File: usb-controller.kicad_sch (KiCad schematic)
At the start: 47 parts, among them Q1502 PJE138K, Q1503 PJE138K, U1501 UPD720201K8-701-BAC-A, U1502 W25Q80DV_USON, Y1501 Resonator_24MHz_ECX-1247

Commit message: [#100501] Reannotate schematic
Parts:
- renumbered C1501 to C105, C1502 to C106, C1503 to C107, C1504 to C108, C1505 to C109, C1506 to C110, C1507 to C111, C1508 to C112, C1509 to C113, C1510 to C114, C1511 to C115, C1512 to C116, C1513 to C117, C1514 to C118, C1515 to C119, C1516 to C120, C1517 to C121, C1518 to C122, C1519 to C123, C1520 to C124, C1521 to C125, C1522 to C126, C1526 to C127, C1527 to C128, C1524 to C129, FB1501 to FB1, Q1503 to Q2, Q1502 to Q3, R1515 to R153, R1517 to R154, R1514 to R155, R1501 to R156, R1516 to R157, R1512 to R158, R1513 to R159, R1503 to R160, R1504 to R161, R1505 to R162, R1506 to R163, R1507 to R164, R1508 to R165, TP1501 to TP20, TP1502 to TP21, TP1503 to TP22, U1501 to U19, U1502 to U20, Y1501 to Y1

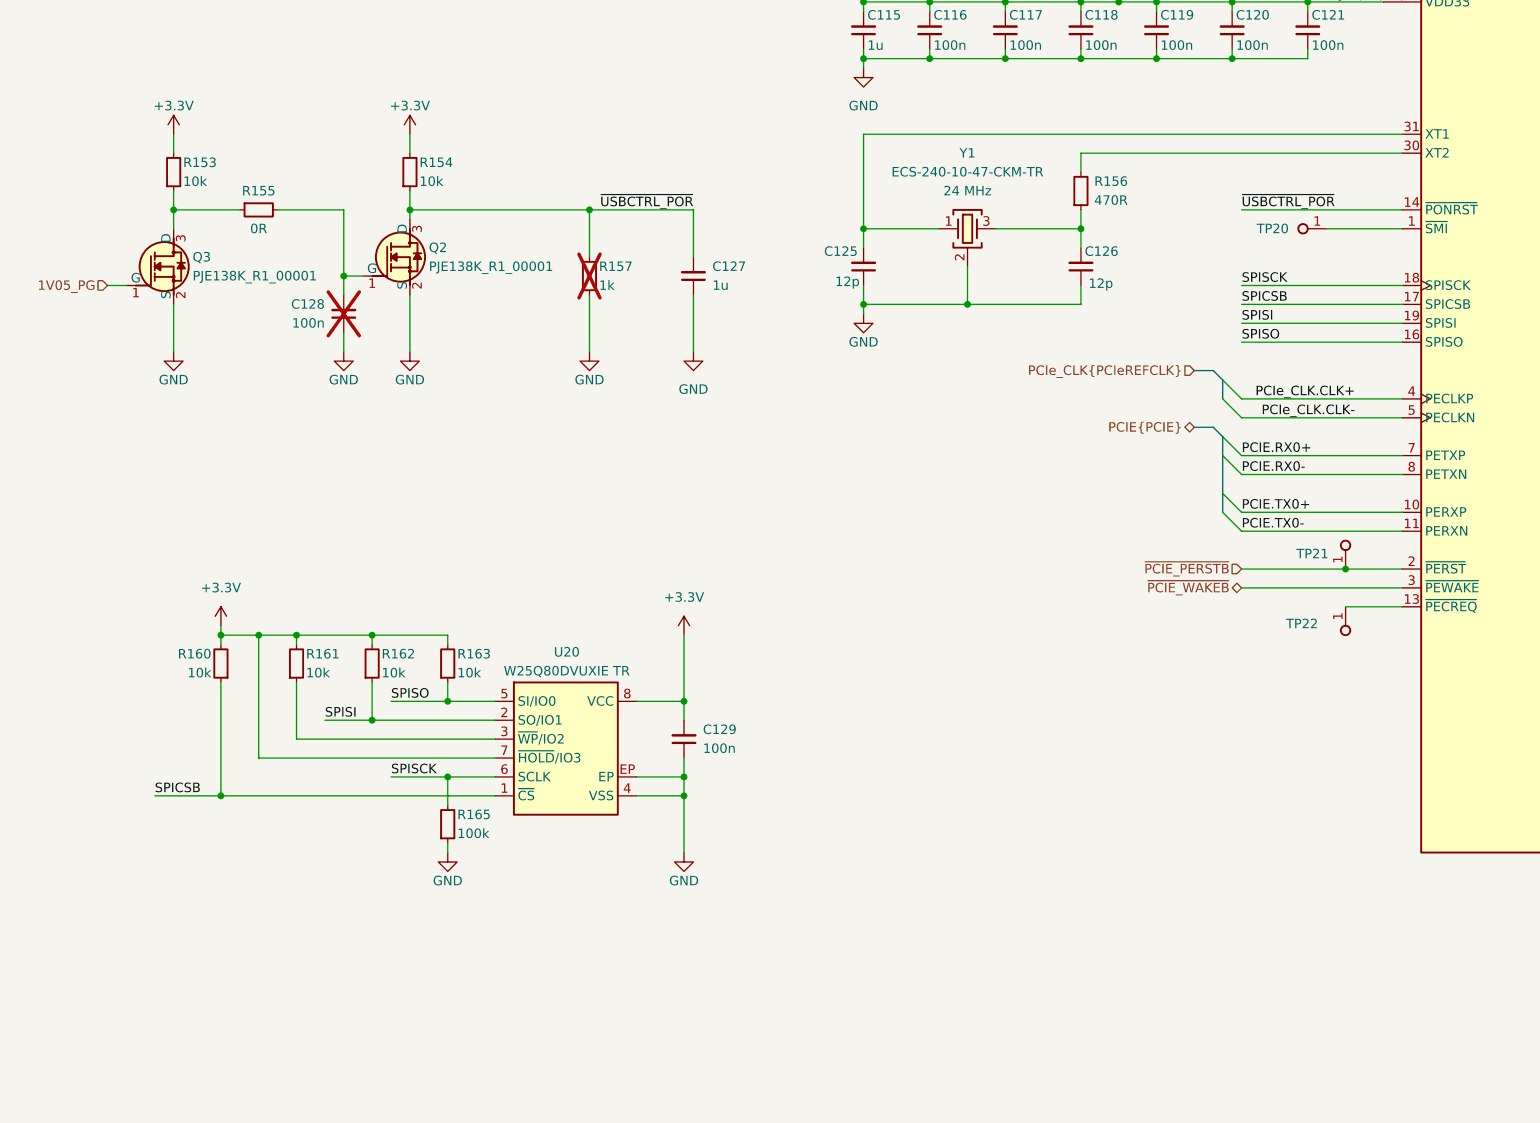
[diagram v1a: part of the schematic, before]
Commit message: [#100501] Add missing pullup resistors for USB controller, add Tag-Connect for its FLASH
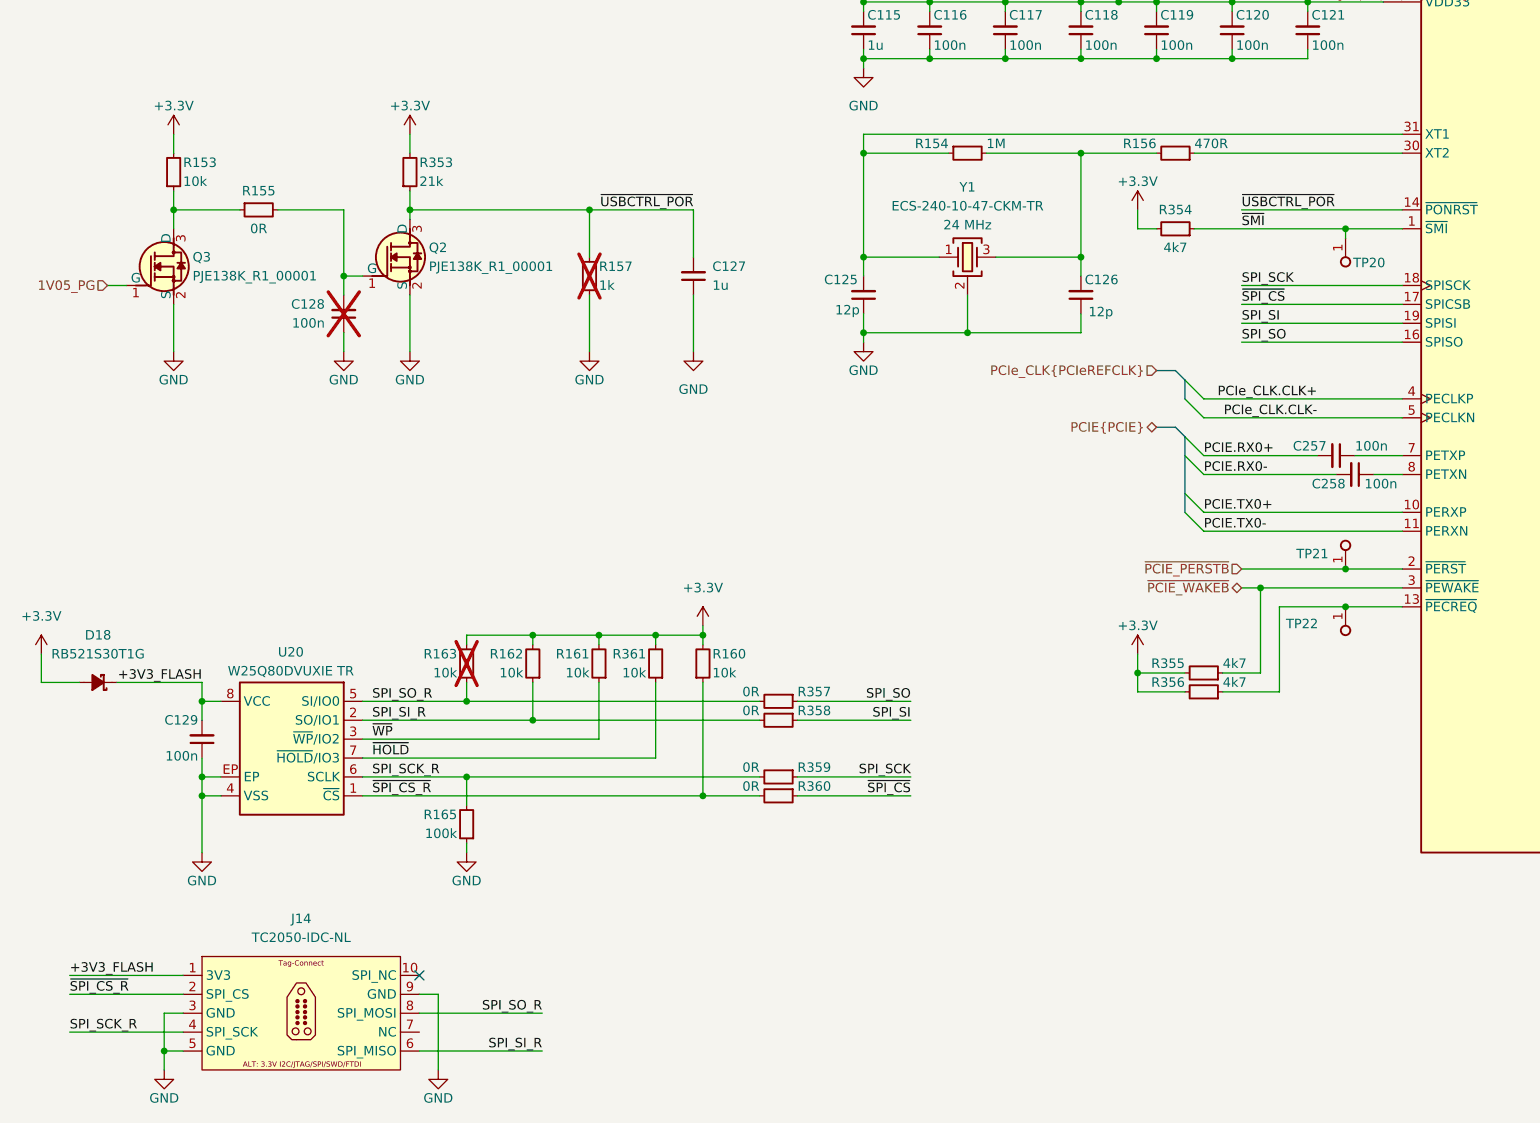
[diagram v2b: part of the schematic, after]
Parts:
- removed R154: R_10k_0402, antmicro-footprints:R_0402_1005Metric, symbol antmicroResistors0402:R_10k_0402
- added C257, C258: C_100n_16V_X7R_0402, antmicro-footprints:C_0402_1005Metric, symbol antmicroCapacitors0402:C_100n_16V_X7R_0402
- added D18: RB521S30T1G, antmicro-footprints:SOD-523, symbol antmicroDiodesRectifiersSingle:RB521S30T1G
- added J14: Tag-Connect_TC2050-IDC-NL_2x5_P1.27mm, antmicro-footprints:Tag-Connect_TC2050-IDC-NL_2x5_P1.27mm, symbol antmicroTestPoints:Tag-Connect_TC2050-IDC-NL_2x5_P1.27mm
- added R154: R_1M_0402, antmicro-footprints:R_0402_1005Metric, symbol antmicroResistors0402:R_1M_0402
- added R353: R_21k_0402, antmicro-footprints:R_0402_1005Metric, symbol antmicroResistors0402:R_21k_0402
- added R354, R355, R356: R_4k7_0402, antmicro-footprints:R_0402_1005Metric, symbol antmicroResistors0402:R_4k7_0402
- added R357, R358, R359, R360: R_0R_0402, antmicro-footprints:R_0402_1005Metric, symbol antmicroResistors0402:R_0R_0402
- added R361: R_10k_0402, antmicro-footprints:R_0402_1005Metric, symbol antmicroResistors0402:R_10k_0402
- R163: now not fitted
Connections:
- net +3.3V: now also D18.2 (A), R353.2, R354.2, R355.2, R356.2, R361.2; no longer C129.2, U20.7 (~{HOLD}/IO3), U20.8 (VCC)
- net GND: now also J14.3, J14.5, J14.9
- net PCIE.RX0+: now also C257.2; no longer U19.7 (PETXP)
- net PCIE.RX0-: now also C258.2; no longer U19.8 (PETXN)
- net ~{PCIE_WAKEB}: now also R355.1
- net ~{USBCTRL_POR}: now also R353.1
- net at C125.2, U19.31 (XT1), Y1.1: now also R154.1
- net at C126.2, Y1.3: now also R156.2, R154.2; no longer R156.1
- net at TP22.1, U19.13 (~{PECREQ}): now also R356.1
- net ~{SMI}: now reaches TP20.1, U19.1 (~{SMI})
- net ~{SMI}: now also R354.1
- net at U19.30 (XT2): now also R156.1; no longer R156.2
- net ~{WP}: now reaches R161.1, U20.3 (~{WP}/IO2)
- net SPICSB renamed ~{SPI_CS_R}
- net ~{SPI_CS_R}: now also J14.2, R360.2; no longer U19.17 (SPICSB)
- net SPISCK renamed SPI_SCK_R
- net SPI_SCK_R: now also J14.4, R359.2; no longer U19.18 (SPISCK)
- net SPISI renamed SPI_SI_R
- net SPI_SI_R: now also J14.6, R358.2; no longer U19.19 (SPISI)
- net SPISO renamed SPI_SO_R
- net SPI_SO_R: now also J14.8, R357.2; no longer U19.16 (SPISO)
- new net: C258.1, U19.8 (PETXN)
- new net: C257.1, U19.7 (PETXP)
- new net +3V3_FLASH: C129.2, D18.1 (C), J14.1, U20.8 (VCC)
- new net SPI_SCK: R359.1, U19.18 (SPISCK)
- new net SPI_SI: R358.1, U19.19 (SPISI)
- new net SPI_SO: R357.1, U19.16 (SPISO)
- new net ~{HOLD}: R361.1, U20.7 (~{HOLD}/IO3)
- new net ~{SPI_CS}: R360.1, U19.17 (SPICSB)
- no-connect marks 6 -> 7
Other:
- moved on the sheet: C125, C126, C129, R160, R161, R162, R165, TP20, U20, Y1

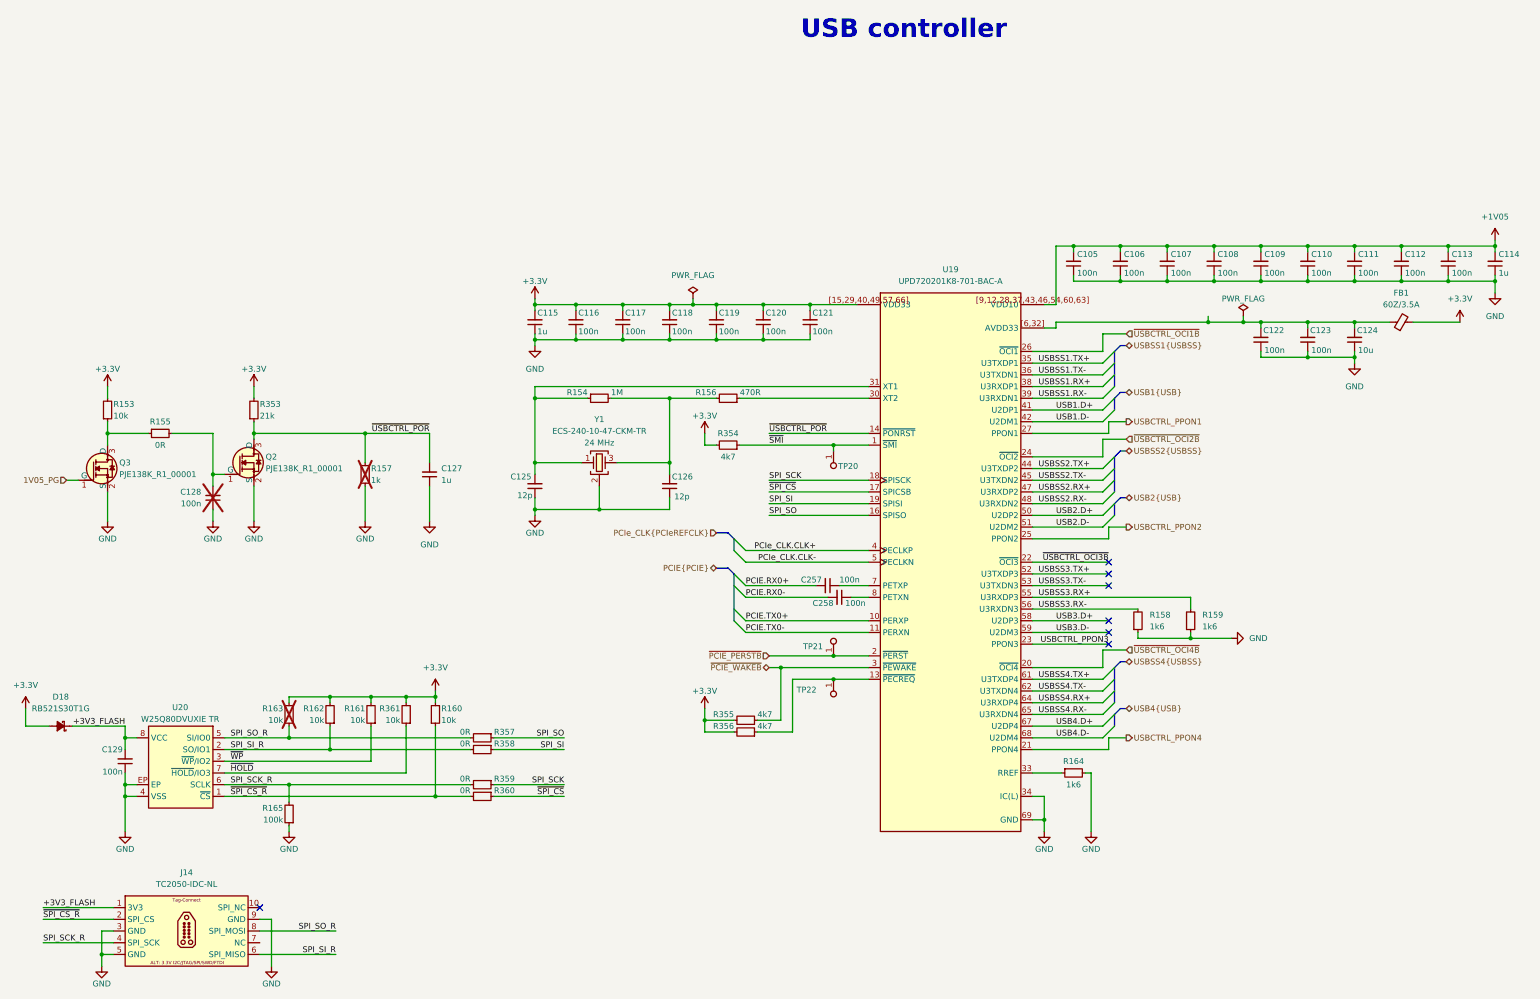
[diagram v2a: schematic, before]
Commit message: [#100501] Improve USB controller schematic readability
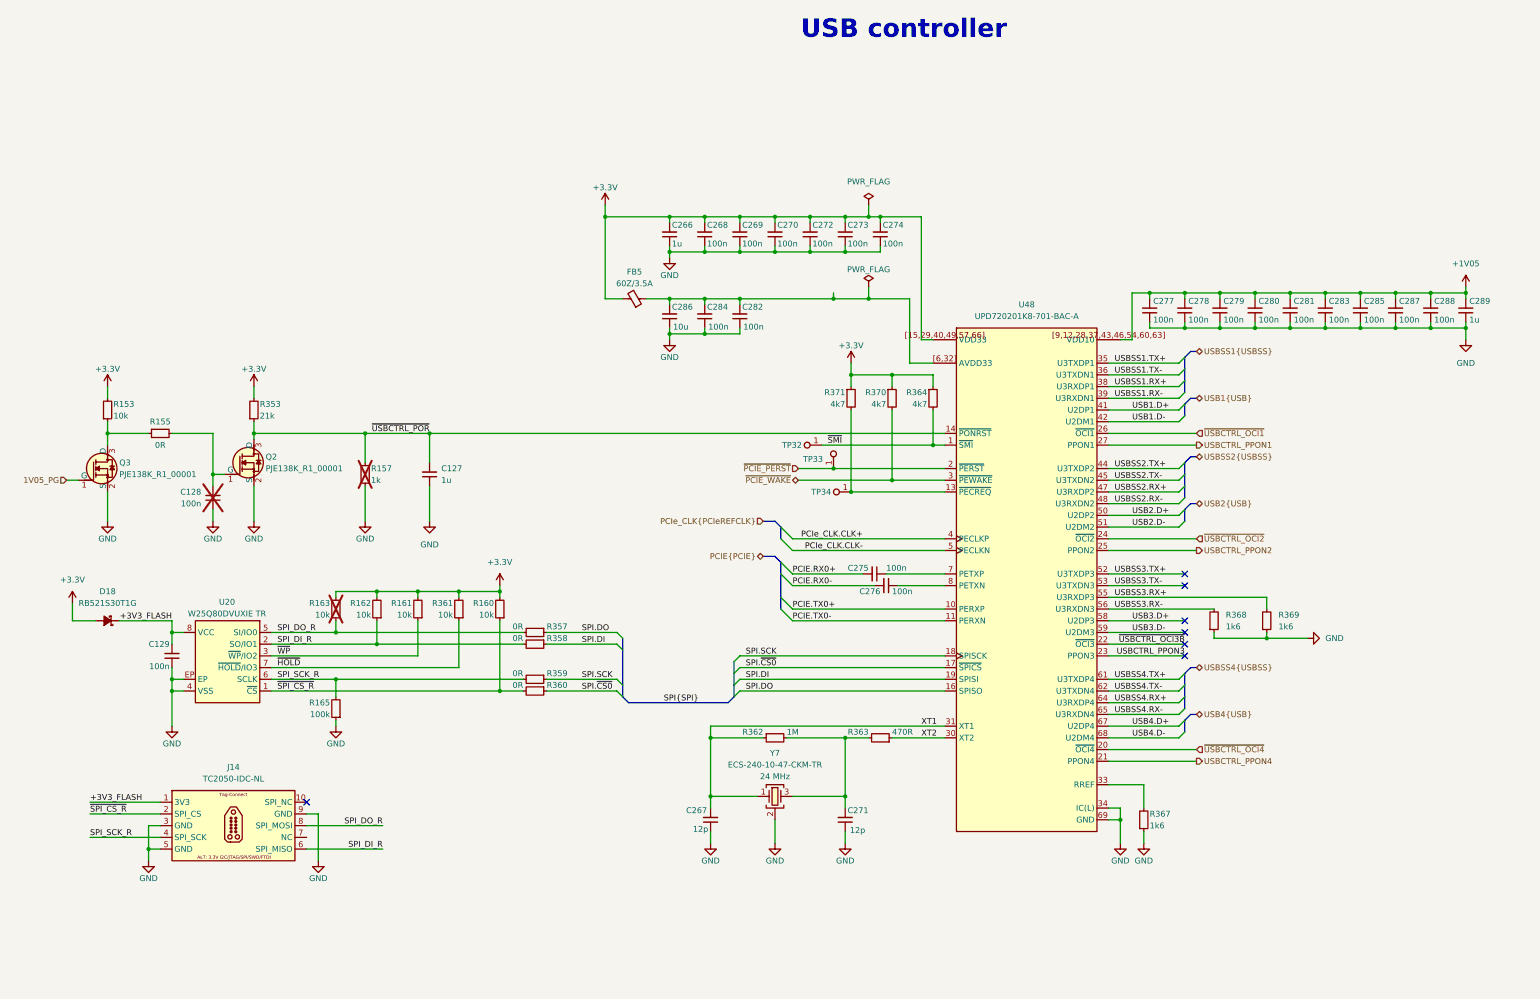
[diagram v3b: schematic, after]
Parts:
- removed C105, C106, C107, C108, C109, C110, C111, C112, C113, C116, C117, C118, C119, C120, C121, C122, C123, C257, C258: C_100n_16V_X7R_0402, antmicro-footprints:C_0402_1005Metric, symbol antmicroCapacitors0402:C_100n_16V_X7R_0402
- removed C114, C115: C_1u_10V_X7R_0402, antmicro-footprints:C_0402_1005Metric, symbol antmicroCapacitors0402:C_1u_10V_X7R_0402
- removed C124: C_10u_6.3V_0402, antmicro-footprints:C_0402_1005Metric, symbol antmicroCapacitors0402:C_10u_6.3V_0402
- removed C125, C126: C_12p_0402, antmicro-footprints:C_0402_1005Metric, symbol antmicroCapacitors0402:C_12p_0402
- removed FB1: FB_60Z_3.5A_Murata-BLM21PG_0805, antmicro-footprints:FB_0805_2012Metric, symbol antmicroFerriteBeadsandChips:FB_60Z_3.5A_Murata-BLM21PG_0805
- removed R154: R_1M_0402, antmicro-footprints:R_0402_1005Metric, symbol antmicroResistors0402:R_1M_0402
- removed R156: R_470R_0402, antmicro-footprints:R_0402_1005Metric, symbol antmicroResistors0402:R_470R_0402
- removed R158, R159, R164: R_1k6_0402, antmicro-footprints:R_0402_1005Metric, symbol antmicroResistors0402:R_1k6_0402
- removed R354, R355, R356: R_4k7_0402, antmicro-footprints:R_0402_1005Metric, symbol antmicroResistors0402:R_4k7_0402
- removed TP20, TP21, TP22: TP_1mm_SMD, antmicro-footprints:TP_SMD_1mm, symbol antmicroTestPoints:TP_1mm_SMD
- removed U19: UPD720201K8-701-BAC-A, antmicro-footprints:QFN-68-1EP_8x8mm_P0.4mm, symbol antmicroInterfaceControllers:UPD720201K8-701-BAC-A
- removed Y1: Resonator_24MHz_ECX-1247, antmicro-footprints:Resonator_SMD_ECS_ECX-1247_1.6x1.2x0.3mm, symbol antmicroResonators:Resonator_24MHz_ECX-1247
- added C266, C289: C_1u_10V_X7R_0402, antmicro-footprints:C_0402_1005Metric, symbol antmicroCapacitors0402:C_1u_10V_X7R_0402
- added C267, C271: C_12p_0402, antmicro-footprints:C_0402_1005Metric, symbol antmicroCapacitors0402:C_12p_0402
- added C268, C269, C270, C272, C273, C274, C275, C276, C277, C278, C279, C280, C281, C282, C283, C284, C285, C287, C288: C_100n_16V_X7R_0402, antmicro-footprints:C_0402_1005Metric, symbol antmicroCapacitors0402:C_100n_16V_X7R_0402
- added C286: C_10u_6.3V_0402, antmicro-footprints:C_0402_1005Metric, symbol antmicroCapacitors0402:C_10u_6.3V_0402
- added FB5: FB_60Z_3.5A_Murata-BLM21PG_0805, antmicro-footprints:FB_0805_2012Metric, symbol antmicroFerriteBeadsandChips:FB_60Z_3.5A_Murata-BLM21PG_0805
- added R362: R_1M_0402, antmicro-footprints:R_0402_1005Metric, symbol antmicroResistors0402:R_1M_0402
- added R363: R_470R_0402, antmicro-footprints:R_0402_1005Metric, symbol antmicroResistors0402:R_470R_0402
- added R364, R370, R371: R_4k7_0402, antmicro-footprints:R_0402_1005Metric, symbol antmicroResistors0402:R_4k7_0402
- added R367, R368, R369: R_1k6_0402, antmicro-footprints:R_0402_1005Metric, symbol antmicroResistors0402:R_1k6_0402
- added TP32, TP33, TP34: TP_1mm_SMD, antmicro-footprints:TP_SMD_1mm, symbol antmicroTestPoints:TP_1mm_SMD
- added U48: UPD720201K8-701-BAC-A, antmicro-footprints:QFN-68-1EP_8x8mm_P0.4mm, symbol antmicroInterfaceControllers:UPD720201K8-701-BAC-A
- added Y7: Resonator_24MHz_ECX-1247, antmicro-footprints:Resonator_SMD_ECS_ECX-1247_1.6x1.2x0.3mm, symbol antmicroResonators:Resonator_24MHz_ECX-1247
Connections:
- net +1V05: now also C277.2, C278.2, C279.2, C280.2, C281.2, C283.2, C285.2, C287.2, C288.2, C289.2, U48.[9,12,28,37,43,46,54,60,63] (VDD10)
- net +3.3V: now also C266.2, C268.2, C269.2, C270.2, C272.2, C273.2, C274.2, FB5.2, R364.1, R370.1, R371.1, U48.[15,29,40,49,57,66] (VDD33)
- net GND: now also C266.1, C267.1, C268.1, C269.1, C270.1, C271.1, C272.1, C273.1, C274.1, C277.1, C278.1, C279.1, C280.1, C281.1, C282.1, C283.1, C284.1, C285.1, C286.1, C287.1, C288.1, C289.1, R367.1, R368.1, R369.1, U48.34 (IC(L)), U48.69 (GND), Y7.2 (SH), Y7.4 (SH)
- net PCIE.RX0+: now also C275.2
- net PCIE.RX0-: now also C276.2
- net PCIE.TX0+: now also U48.10 (PERXP)
- net PCIE.TX0-: now also U48.11 (PERXN)
- net PCIe_CLK.CLK+: now also U48.4 (PECLKP)
- net PCIe_CLK.CLK-: now also U48.5 (PECLKN)
- net USB1.D+: now also U48.41 (U2DP1)
- net USB1.D-: now also U48.42 (U2DM1)
- net USB2.D+: now also U48.50 (U2DP2)
- net USB2.D-: now also U48.51 (U2DM2)
- net USB3.D+: now also U48.58 (U2DP3)
- net USB3.D-: now also U48.59 (U2DM3)
- net USB4.D+: now also U48.67 (U2DP4)
- net USB4.D-: now also U48.68 (U2DM4)
- net USBCTRL_PPON1: now also U48.27 (PPON1)
- net USBCTRL_PPON2: now also U48.25 (PPON2)
- net USBCTRL_PPON3: now also U48.23 (PPON3)
- net USBCTRL_PPON4: now also U48.21 (PPON4)
- net USBSS1.RX+: now also U48.38 (U3RXDP1)
- net USBSS1.RX-: now also U48.39 (U3RXDN1)
- net USBSS1.TX+: now also U48.35 (U3TXDP1)
- net USBSS1.TX-: now also U48.36 (U3TXDN1)
- net USBSS2.RX+: now also U48.47 (U3RXDP2)
- net USBSS2.RX-: now also U48.48 (U3RXDN2)
- net USBSS2.TX+: now also U48.44 (U3TXDP2)
- net USBSS2.TX-: now also U48.45 (U3TXDN2)
- net USBSS3.RX+: now also R369.2, U48.55 (U3RXDP3)
- net USBSS3.RX-: now also R368.2, U48.56 (U3RXDN3)
- net USBSS3.TX+: now also U48.52 (U3TXDP3)
- net USBSS3.TX-: now also U48.53 (U3TXDN3)
- net USBSS4.RX+: now also U48.64 (U3RXDP4)
- net USBSS4.RX-: now also U48.65 (U3RXDN4)
- net USBSS4.TX+: now also U48.61 (U3TXDP4)
- net USBSS4.TX-: now also U48.62 (U3TXDN4)
- net ~{SMI}: now also R364.2, TP32.1, U48.1 (~{SMI})
- net ~{USBCTRL_OCI3B}: now also U48.22 (~{OCI3})
- net ~{USBCTRL_POR}: now also U48.14 (~{PONRST})
- net SPI_SCK renamed SPI.SCK
- net SPI.SCK: now also U48.18 (SPISCK)
- net SPI_SI renamed SPI.DI
- net SPI.DI: now also U48.19 (SPISI)
- net SPI_SI_R renamed SPI_DI_R
- net SPI_SO renamed SPI.DO
- net SPI.DO: now also U48.16 (SPISO)
- net SPI_SO_R renamed SPI_DO_R
- net ~{SPI_CS} renamed SPI.~{CS0}
- net SPI.~{CS0}: now also U48.17 (~{SPICS})
- new net: C271.2, R362.2, R363.2, Y7.3
- new net: C282.2, C284.2, C286.2, FB5.1, U48.[6,32] (AVDD33)
- new net: C275.1, U48.7 (PETXP)
- new net: C276.1, U48.8 (PETXN)
- new net: R371.2, TP34.1, U48.13 (~{PECREQ})
- new net: R367.2, U48.33 (RREF)
- new net XT1: C267.2, R362.1, U48.31 (XT1), Y7.1
- new net XT2: R363.1, U48.30 (XT2)
- new net ~{PCIE_PERST}: TP33.1, U48.2 (~{PERST})
- new net ~{PCIE_WAKE}: R370.2, U48.3 (~{PEWAKE})
- new net ~{USBCTRL_OCI1}: U48.26 (~{OCI1})
- new net ~{USBCTRL_OCI2}: U48.24 (~{OCI2})
- new net ~{USBCTRL_OCI4}: U48.20 (~{OCI4})
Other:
- moved on the sheet: C129, D18, J14, R160, R161, R162, R163, R165, R357, R358, R359, R360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

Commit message: [#100501] Pullup unused OCI from USB controller, fix 3V3 rail name on USB controller
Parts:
- added R166, R219, R220: R_10k_0402, antmicro-footprints:R_0402_1005Metric, symbol antmicroResistors0402:R_10k_0402
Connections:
- net ~{USBCTRL_OCI1}: now also R219.1
- net ~{USBCTRL_OCI3B}: now also R166.1
- net ~{USBCTRL_OCI4}: now also R220.1
- net +3.3V renamed +3V3
- net +3V3: now also R166.2, R219.2, R220.2
- no-connect marks 7 -> 6
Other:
- note added: "Pullup unused OCI pins"
- moved on the sheet: D18, R368, R369
